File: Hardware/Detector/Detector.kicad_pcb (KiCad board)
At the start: 4 copper layers, 50 x 48 mm, 138 parts, among them J1 Conn_Coaxial, J4 Conn_Coaxial, J5 Conn_Coaxial, J6 Conn_Coaxial, J7 Conn_Coaxial, U1 OPA145ID, U10 OPA145ID, U11 OPA145ID, U12 OPA145ID, U13 OPA145ID, U14 OPA145ID, U15 OPA145ID, U2 OPA145ID, U3 OPA145ID, U4 OPA145ID, U5 OPA145ID, U6 OPA145ID, U7 OPA145ID, U8 OPA145ID, U9 OPA145ID

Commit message: transition to KiCad6
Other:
- net class Default removed

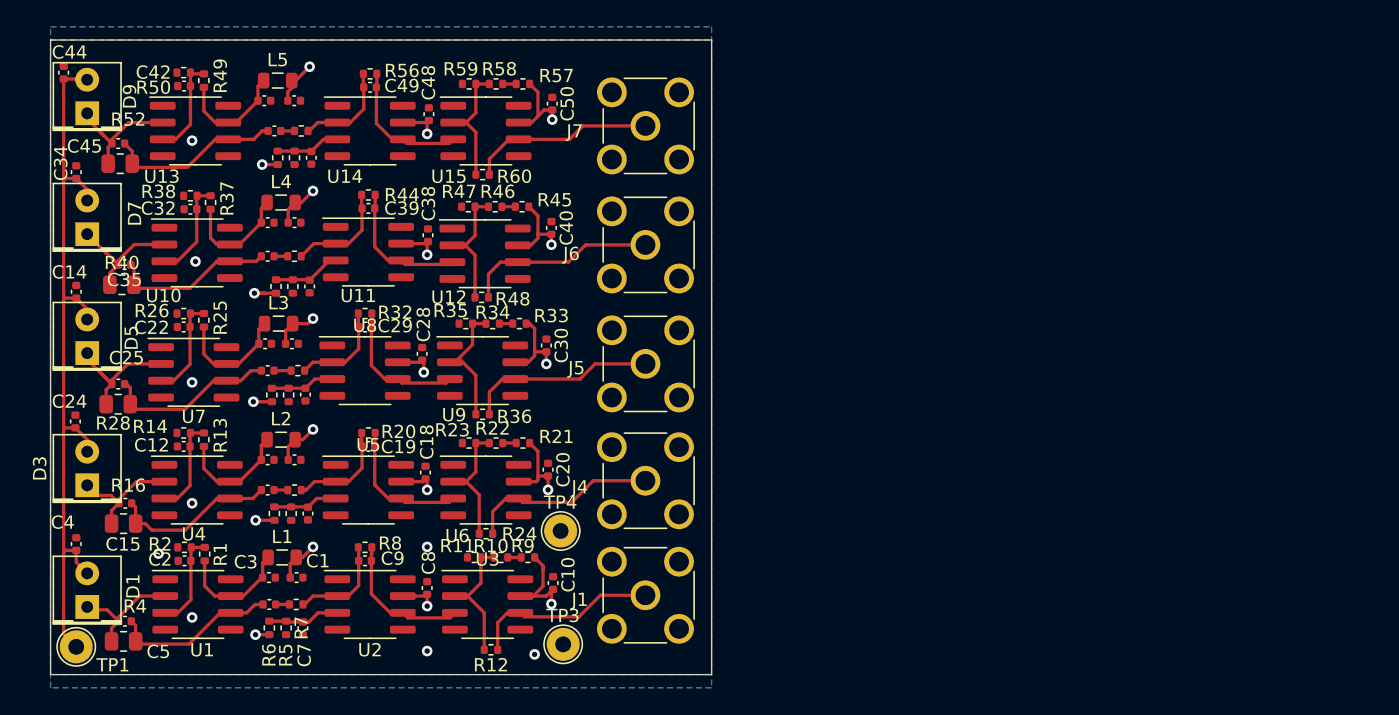
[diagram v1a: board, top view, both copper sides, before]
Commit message: further implementation of low cost version
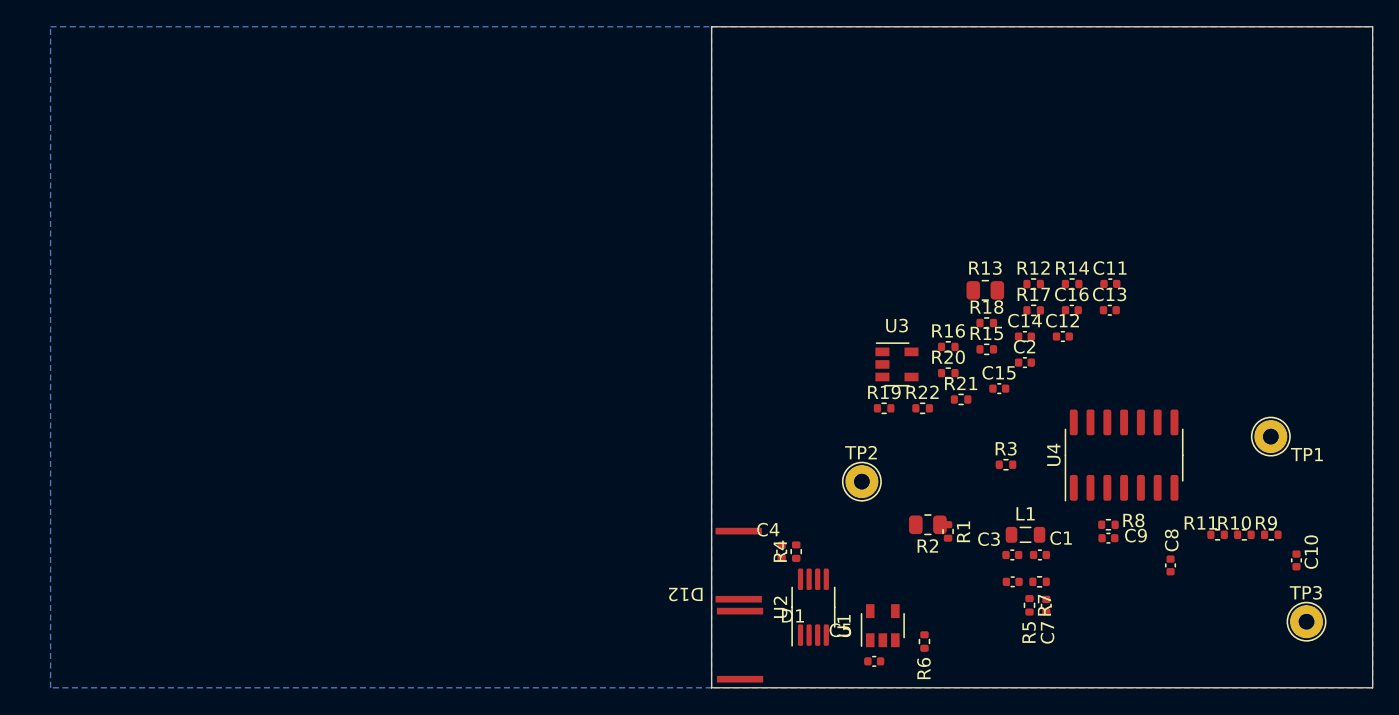
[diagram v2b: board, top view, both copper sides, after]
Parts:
- removed C17, C18, C20, C21, C22, C23, C24, C27, C28, C30, C31, C32, C33, C34, C37, C38, C40, C41, C42, C43, C44, C47, C48, C50: 100n, Capacitor_SMD:C_0402_1005Metric
- removed C19, C29, C39, C49: 4p7+2p2, Capacitor_SMD:C_0402_1005Metric
- removed C25, C35, C45: 2p2, Capacitor_SMD:C_0402_1005Metric
- removed C26, C36, C46: 1n, Capacitor_SMD:C_0402_1005Metric
- removed D3, D5, D7, D9: BPW34, LED_THT:LED_Rectangular_W5.0mm_H5.0mm
- removed J1, J4, J5, J6, J7: Conn_Coaxial, Connector_Coaxial:SMA_Molex_73251-2200_Horizontal
- removed L2, L3, L4, L5: u68, Inductor_SMD:L_0805_2012Metric
- removed R23, R25, R26, R29, R30, R31, R33, R35, R37, R38, R41, R42, R43, R45, R47, R49, R50, R53, R54, R55, R57, R59: 10k, Resistor_SMD:R_0402_1005Metric
- removed R24, R36, R48, R60: not mounted, Resistor_SMD:R_0402_1005Metric
- removed R28, R40, R52: 10G, Resistor_SMD:R_0805_2012Metric
- removed R32, R44, R56: 10M, Resistor_SMD:R_0402_1005Metric
- removed R34, R46, R58: 0R, Resistor_SMD:R_0402_1005Metric
- removed TP4: TestPoint, TestPoint:TestPoint_THTPad_D2.5mm_Drill1.2mm
- removed U10, U11, U12, U13, U14, U15, U5, U6, U7, U8, U9: OPA145ID, Package_SO:SOIC-8_3.9x4.9mm_P1.27mm
- added D12: BPW34, DiscretePixelDetectorForRadiationAnalysis:BPW 34 OSRAM, F.Cu at (103.8, 87.9)
- added R15: 10k, Resistor_SMD:R_0402_1005Metric, F.Cu at (120.8, 74.4)
- added R3: 10k, Resistor_SMD:R_0402_1005Metric, F.Cu at (122.3, 83.1)
- added TP2: TestPoint, TestPoint:TestPoint_THTPad_D2.5mm_Drill1.2mm, F.Cu at (111.4, 84.4)
- C1, C11: value 100n -> 2p2
- C12, C3: value 100n -> 1n
- C15: value 2p2 -> 4p7+2p2
- C16: value 1n -> 100n
- C5: value 2p2 -> 100n
- C6: value 1n -> 4p7+2p2
- C9: value 4p7+2p2 -> 100n
- D1: footprint LED_THT:LED_Rectangular_W5.0mm_H5.0mm -> DiscretePixelDetectorForRadiationAnalysis:BPW 34 OSRAM
- R10, R22: value 0R -> 10k
- R12: value not mounted -> 10k
- R13, R2: value 10k -> 10G; footprint Resistor_SMD:R_0402_1005Metric -> Resistor_SMD:R_0805_2012Metric
- R16: value 10G -> 0R; footprint Resistor_SMD:R_0805_2012Metric -> Resistor_SMD:R_0402_1005Metric
- R19: value 10k -> 10M
- R20: value 10M -> not mounted
- R4: value 10G -> 10k; footprint Resistor_SMD:R_0805_2012Metric -> Resistor_SMD:R_0402_1005Metric
- R5: value 10k -> 0R
- R9: value 10k -> not mounted
- U1, U3: value OPA145ID -> AS321; footprint Package_SO:SOIC-8_3.9x4.9mm_P1.27mm -> Package_TO_SOT_SMD:SOT-23-5
- U2: value OPA145ID -> MCP6477; footprint Package_SO:SOIC-8_3.9x4.9mm_P1.27mm -> Package_SO:MSOP-8_3x3mm_P0.65mm
- U4: value OPA145ID -> AS339MTR-G1; footprint Package_SO:SOIC-8_3.9x4.9mm_P1.27mm -> Package_SO:SO-14_3.9x8.65mm_P1.27mm
- moved TP1 91.7 mm to (142.3, 81.0)
- moved C14 71.8 mm to (123.7, 73.4), turned to 0 degrees
- moved U4 70.2 mm to (131.2, 82.4), turned to 90 degrees
- moved R14 68.1 mm to (127.3, 69.5), turned to 0 degrees
- moved C12 67.0 mm to (126.6, 73.4), turned to 0 degrees
- moved C15 66.7 mm to (121.8, 77.4), turned to 0 degrees
- moved C2 65.3 mm to (123.7, 75.4), turned to 0 degrees
- moved C13 64.7 mm to (130.1, 71.4)
- moved R16 63.8 mm to (117.9, 74.2)
- moved C11 63.1 mm to (130.2, 69.5)
- moved C16 62.3 mm to (127.2, 71.4), turned to 0 degrees
- moved R13 60.2 mm to (120.7, 69.9), turned to 0 degrees
- moved R17 57.5 mm to (124.4, 71.5), turned to 0 degrees
- moved C5 56.8 mm to (112.3, 98.0), turned to 0 degrees
- moved C10 56.3 mm to (144.2, 90.4)
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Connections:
- C1 pad 1: VCC -> Net-(C1-Pad1)
- C1 pad 2: GND -> Net-(C1-Pad2)
- C10 pad 1: GND -> VCC
- C10 pad 2: VCC -> GND
- C11 pad 1: VCC -> Net-(U2-Pad7)
- C11 pad 2: GND -> Net-(U2-Pad6)
- C12 pad 2: GND -> Net-(U2-Pad7)
- C13 pad 1: Net-(C13-Pad1) -> Net-(U2-Pad5)
- C14 pad 1: GND -> Net-(C14-Pad1)
- C14 pad 2: PHOTODIODE_POLARIZATION -> GND
- C15 pad 1: Net-(C15-Pad1) -> Net-(U4-Pad7)
- C16 pad 1: Net-(C16-Pad1) -> GND
- C16 pad 2: Net-(C15-Pad1) -> PHOTODIODE_POLARIZATION
- C2 pad 1: Net-(C2-Pad1) -> VCC
- C3 pad 2: GND -> Net-(C1-Pad1)
- C4 pad 1: GND -> Net-(C4-Pad1)
- C4 pad 2: PHOTODIODE_POLARIZATION -> GND
- C5 pad 2: Net-(C5-Pad2) -> GND
- C6 pad 2: Net-(C5-Pad1) -> Net-(C6-Pad2)
- C7 pad 1: Net-(C7-Pad1) -> GND
- C7 pad 2: GND -> PHOTODIODE_POLARIZATION
- C8 pad 1: GND -> VCC
- C8 pad 2: VCC -> GND
- C9 pad 1: Net-(C9-Pad1) -> /Detector1and2/IMPUT_OPAMP_VCC
- C9 pad 2: Net-(C9-Pad2) -> GND
- D1 pad 1: Net-(C5-Pad2) -> Net-(C1-Pad2)
- L1 pad 1: Net-(C3-Pad1) -> /Detector1and2/IMPUT_OPAMP_VCC
- R1 pad 1: Net-(C3-Pad1) -> VCC
- R1 pad 2: Net-(C2-Pad1) -> Net-(R1-Pad2)
- R10 pad 1: Net-(R10-Pad1) -> Net-(C5-Pad1)
- R10 pad 2: Net-(R10-Pad2) -> GND
- R11 pad 1: Net-(R10-Pad2) -> Net-(R11-Pad1)
- R12 pad 1: Net-(J1-Pad1) -> VCC
- R12 pad 2: Net-(R10-Pad2) -> Net-(R12-Pad2)
- R13 pad 1: Net-(C13-Pad1) -> Net-(U2-Pad6)
- R13 pad 2: Net-(C12-Pad1) -> Net-(U2-Pad7)
- R14 pad 1: Net-(C12-Pad1) -> VCC
- R14 pad 2: GND -> Net-(C14-Pad1)
- R16 pad 1: Net-(C15-Pad2) -> Net-(R12-Pad2)
- R16 pad 2: Net-(C15-Pad1) -> Net-(U4-Pad6)
- R17 pad 1: Net-(C19-Pad2) -> Net-(C15-Pad2)
- R17 pad 2: Net-(C16-Pad1) -> Net-(C12-Pad1)
- R18 pad 1: VCC -> Net-(U2-Pad5)
- R18 pad 2: Net-(C17-Pad1) -> GND
- R19 pad 1: Net-(C17-Pad1) -> Net-(U4-Pad7)
- R19 pad 2: GND -> Net-(C15-Pad2)
- R2 pad 1: Net-(C2-Pad1) -> Net-(C1-Pad2)
- R2 pad 2: GND -> Net-(C1-Pad1)
- R20 pad 1: Net-(C19-Pad1) -> PIXEL_2
- R20 pad 2: Net-(C19-Pad2) -> Net-(U4-Pad6)
- R21 pad 1: VCC -> Net-(C14-Pad1)
- R21 pad 2: Net-(R21-Pad2) -> GND
- R22 pad 1: Net-(R21-Pad2) -> Net-(U4-Pad6)
- R22 pad 2: Net-(R22-Pad2) -> GND
- R4 pad 1: Net-(C5-Pad2) -> /Detector1and2/IMPUT_OPAMP_VCC
- R4 pad 2: Net-(C5-Pad1) -> Net-(C4-Pad1)
- R5 pad 1: Net-(C9-Pad2) -> Net-(R1-Pad2)
- R5 pad 2: Net-(C6-Pad1) -> Net-(R11-Pad1)
- R6 pad 1: VCC -> Net-(C6-Pad2)
- R6 pad 2: Net-(C7-Pad1) -> Net-(C3-Pad1)
- R7 pad 1: Net-(C7-Pad1) -> Net-(C4-Pad1)
- R8 pad 1: Net-(C9-Pad1) -> Net-(C6-Pad1)
- R8 pad 2: Net-(C9-Pad2) -> Net-(C6-Pad2)
- R9 pad 1: VCC -> PIXEL_1
- R9 pad 2: Net-(R10-Pad1) -> Net-(R11-Pad1)
- TP1 pad 1: PHOTODIODE_POLARIZATION -> VCC
- TP3 pad 1: VCC -> PHOTODIODE_POLARIZATION
- U1 pad 1: (no net) -> Net-(C5-Pad1)
- U1 pad 2: Net-(C5-Pad2) -> GND
- U1 pad 3: Net-(C2-Pad1) -> Net-(C6-Pad2)
- U1 pad 4: GND -> Net-(C6-Pad1)
- U1 pad 5: (no net) -> VCC
- U2 pad 1: (no net) -> Net-(C1-Pad1)
- U2 pad 2: Net-(C9-Pad2) -> Net-(C1-Pad2)
- U2 pad 3: Net-(C7-Pad1) -> Net-(C4-Pad1)
- U2 pad 5: (no net) -> Net-(U2-Pad5)
- U2 pad 6: Net-(C9-Pad1) -> Net-(U2-Pad6)
- U2 pad 7: VCC -> Net-(U2-Pad7)
- U2 pad 8: (no net) -> /Detector1and2/IMPUT_OPAMP_VCC
- U3 pad 1: (no net) -> Net-(C14-Pad1)
- U3 pad 2: Net-(R10-Pad2) -> (no net)
- U3 pad 3: Net-(C9-Pad1) -> Net-(C15-Pad2)
- U3 pad 4: GND -> Net-(U4-Pad7)
- U4 pad 1: (no net) -> PIXEL_2
- U4 pad 2: Net-(C15-Pad2) -> PIXEL_1
- U4 pad 3: Net-(C12-Pad1) -> VCC
- U4 pad 4: GND -> Net-(R11-Pad1)
- U4 pad 5: (no net) -> Net-(C6-Pad1)
- U4 pad 6: Net-(C15-Pad1) -> Net-(U4-Pad6)
- U4 pad 7: Net-(C13-Pad1) -> Net-(U4-Pad7)
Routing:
- net VCC: track 72.0 -> 0.00 mm, vias 20 -> 0
- net PHOTODIODE_POLARIZATION: track 58.0 -> 0.00 mm
- net Net-(J6-Pad1): track 14.5 -> 0.00 mm
- net Net-(J4-Pad1): track 14.4 -> 0.00 mm
- net Net-(J5-Pad1): track 14.4 -> 0.00 mm
- net Net-(J1-Pad1): track 14.3 -> 0.00 mm
- net Net-(J7-Pad1): track 14.0 -> 0.00 mm
- net Net-(C45-Pad1): track 13.3 -> 0.00 mm
- net Net-(C25-Pad1): track 13.1 -> 0.00 mm
- net Net-(C15-Pad1): track 12.6 -> 0.00 mm
- net Net-(C5-Pad1): track 12.6 -> 0.00 mm
- net Net-(C35-Pad1): track 12.4 -> 0.00 mm
- net Net-(R10-Pad2): track 10.9 -> 0.00 mm
- net Net-(C9-Pad1): track 10.8 -> 0.00 mm
- net Net-(C49-Pad1): track 10.7 -> 0.00 mm
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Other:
- board size 50 x 48 mm -> 50 x 50 mm
